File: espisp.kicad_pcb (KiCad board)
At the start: 2 copper layers, 17.1 x 26.7 mm, 20 parts, among them P1 FTDI_BASIC, SW1 SW_PUSH, SW2 SW_PUSH, U1 ESP-12, U2 AMS1117-3.3

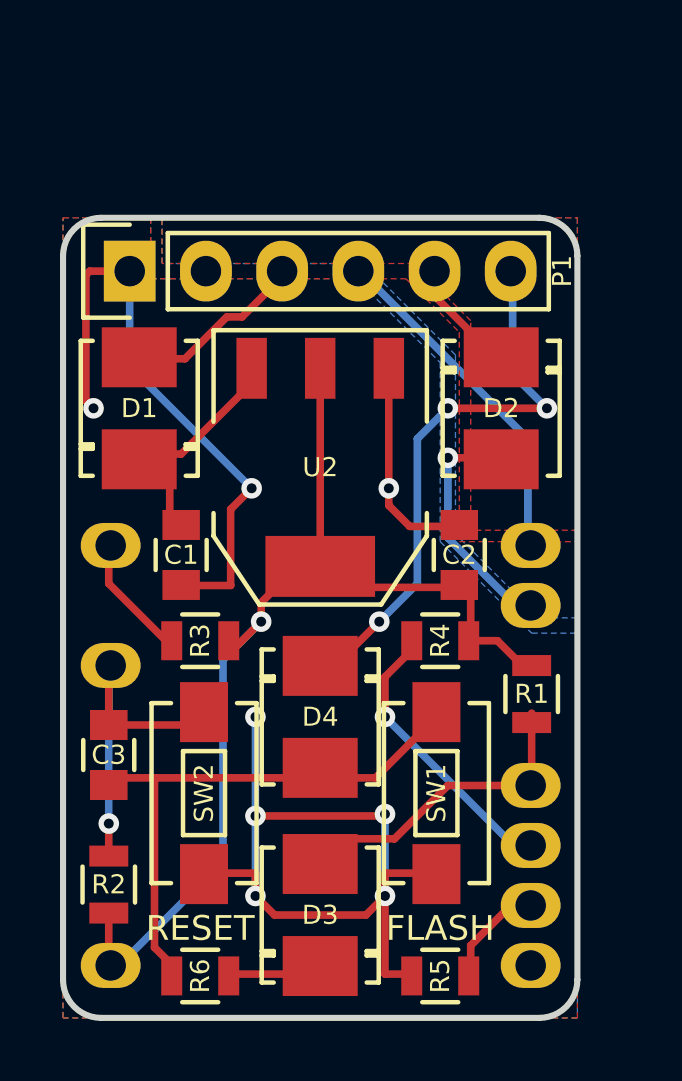
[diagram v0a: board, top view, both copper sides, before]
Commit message: Changed FLASH button to a general GPIO0 button.
First manufacturing.
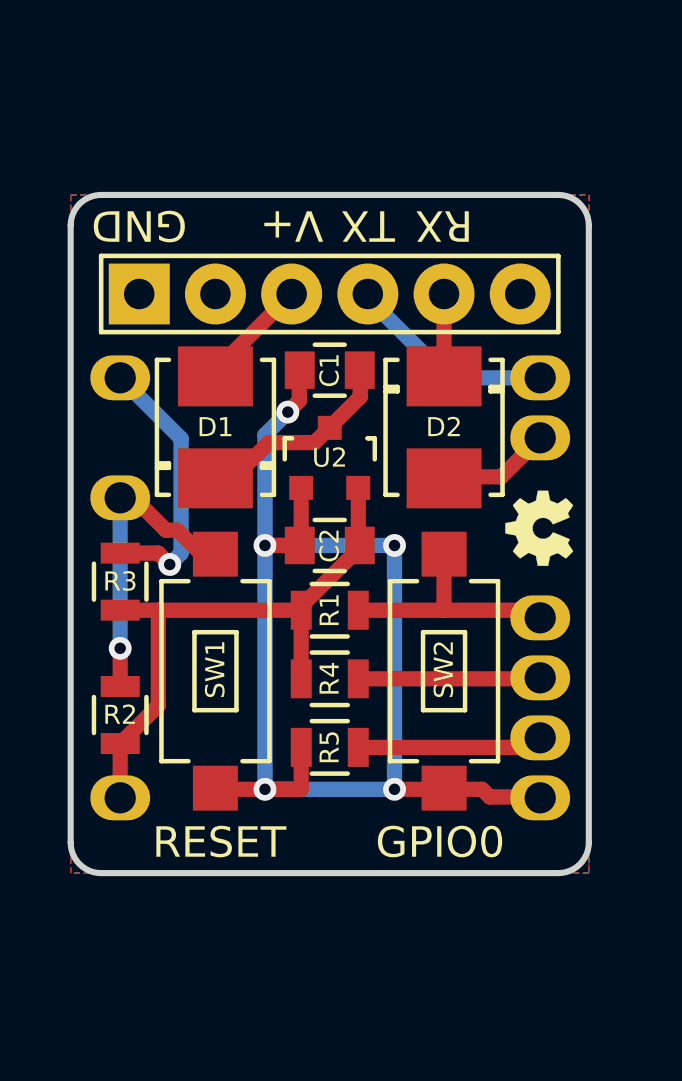
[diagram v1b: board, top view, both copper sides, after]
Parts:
- removed C3: 100nF, Capacitors_SMD:C_0805
- removed D3, D4: 1N4148, Diodes_SMD:DO-214BA
- removed R6: 1K, Resistors_SMD:R_0805
- C1, C2: value CP -> 1uF
- D1, D2: value 1N4148 -> 1N5819
- G***: moved to F.Cu
- P1: footprint Pin_Headers:Pin_Header_Straight_1x06 -> my_footprints:Pin_Header_Simple_1x06
- SW1: value SW_PUSH -> RESET; footprint Buttons_Switches_SMD:SW_SPST_EVQPE1 -> my_footprints:SMD_PUSHBUTTON_3.6x6.0mm
- SW2: value SW_PUSH -> FLASH; footprint Buttons_Switches_SMD:SW_SPST_EVQPE1 -> my_footprints:SMD_PUSHBUTTON_3.6x6.0mm
- U2: value AMS1117-3.3 -> XC6206; footprint TO_SOT_Packages_SMD:SOT-223 -> TO_SOT_Packages_SMD:SOT-23
- moved SW2 8.97 mm to (54.1, 44.3), turned to 0 degrees
- moved R5 8.46 mm to (50.3, 46.9)
- moved SW1 8.41 mm to (46.5, 44.3), turned to 0 degrees
- moved C1 7.90 mm to (50.3, 34.3), turned to 180 degrees
- moved R1 7.29 mm to (50.3, 42.3), turned to 0 degrees
- moved G*** 5.99 mm to (54.5, 39.5), turned to 180 degrees
- moved R2 5.66 mm to (43.3, 45.8)
- moved U1 5.60 mm to (43.3, 34.5)
- moved C2 4.33 mm to (50.3, 40.1), turned to 180 degrees
- moved R4 3.90 mm to (50.3, 44.6), turned to 0 degrees
- moved R3 3.31 mm to (43.3, 41.3), turned to 90 degrees
- moved D1 2.62 mm to (46.5, 36.2)
- moved G*** 2.43 mm to (57.3, 39.6), turned to 90 degrees
- moved D2 2.01 mm to (54.1, 36.2)
- moved P1 0.83 mm to (43.9, 31.8)
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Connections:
- P1 pad 6: /DTR_5V -> (no net)
- SW1 pad 1: Net-(C3-Pad1) -> /CH_PD
- SW2 pad 1: /CH_PD -> /GPIO0
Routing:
- net Net-(C3-Pad1): track 17.0 -> 0.00 mm
- net /DTR_5V: track 16.9 -> 0.00 mm, vias 3 -> 0
- net +3V3: track 33.3 -> 19.8 mm, vias 1 -> 0
- net GND: track 51.1 -> 43.8 mm, vias 8 -> 5
- net /RESET: track 4.14 -> 9.03 mm, vias 0 -> 1
- net /GPIO15: track 2.30 -> 5.97 mm
- net /TXD: track 10.4 -> 7.00 mm
- net /RXD: track 6.30 -> 3.70 mm, vias 1 -> 0
- net /GPIO2: track 8.34 -> 5.97 mm, vias 1 -> 0
- net Net-(D3-Pad1): track 2.03 -> 0.00 mm
- net /VIN_5V: track 4.43 -> 3.05 mm
- net /GPIO0: track 9.25 -> 7.87 mm
- net /CH_PD: track 11.0 -> 10.1 mm
- net Net-(C1-Pad1): track 5.29 -> 5.83 mm
- removed copper zone on B.Cu, net (none)
- removed copper zone on F.Cu, net (none)
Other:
- board size 17.1 x 26.7 mm -> 17.3 x 22.6 mm
- net class Default: clearance 0.2032 -> 0.254; trace_width 0.254 -> 0.508; via_dia 0.6858 -> 0.762; via_drill 0.3302 -> 0.381
- rule trace_clearance: 0.2032 -> 0.254
- board text added: "ESP-ISP"
- board text added: "Rev.4"
- board text added: "V+"
- board text removed: "ESP-12 Antenna"
- board text removed: "ESP-12 ISP"
- board text removed: "FLASH"
- board text removed: "Rv.3"
- board text removed: "VIN"

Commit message: Combine RESET and GPIO0 into one button. (Untested)
Pressing the button should reset the MCU. Pressing and holding the
button for ~5 seconds should make it enter flash mode upon release.

Take a look at /proto/flash.txt to see it in action.
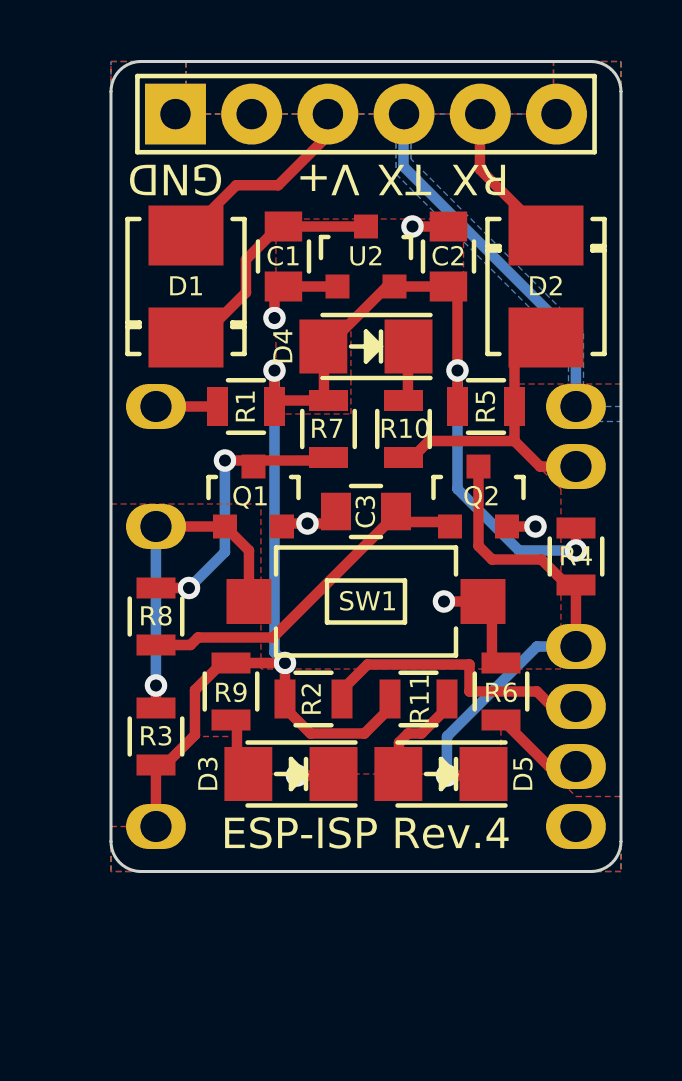
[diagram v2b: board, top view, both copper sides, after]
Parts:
- removed G***: LOGO, my_footprints:Ferret_Logo_0.1in
- removed G***: LOGO, my_footprints:OSHW_Logo_0.1in
- removed SW2: FLASH, my_footprints:SMD_PUSHBUTTON_3.6x6.0mm
- added C3: 2.2uF, Capacitors_SMD:C_0805, F.Cu at (51.5, 39.0)
- added D3: GREEN, LEDs:LED_1206, F.Cu at (49.0, 47.8)
- added D4: GREEN, LEDs:LED_1206, F.Cu at (51.5, 33.5)
- added D5: RED, LEDs:LED_1206, F.Cu at (54.0, 47.8)
- added Q1: 2N7002, TO_SOT_Packages_SMD:SOT-23, F.Cu at (47.8, 38.5)
- added Q2: 2N7002, TO_SOT_Packages_SMD:SOT-23, F.Cu at (55.2, 38.5)
- added R10: 220, Resistors_SMD:R_0805, F.Cu at (52.8, 36.2)
- added R11: 220, Resistors_SMD:R_0805, F.Cu at (53.2, 45.2)
- added R6: 10K, Resistors_SMD:R_0805, F.Cu at (56.0, 45.0)
- added R7: 1M, Resistors_SMD:R_0805, F.Cu at (50.2, 36.2)
- added R8: 1M, Resistors_SMD:R_0805, F.Cu at (44.5, 42.5)
- added R9: 220, Resistors_SMD:R_0805, F.Cu at (47.0, 45.0)
- moved R5 12.5 mm to (55.5, 35.5)
- moved C2 10.4 mm to (54.2, 30.5), turned to 90 degrees
- moved P1 9.65 mm to (51.5, 25.8)
- moved R4 9.16 mm to (58.5, 40.5), turned to 270 degrees
- moved R1 7.34 mm to (47.5, 35.5), turned to 180 degrees
- moved U2 6.82 mm to (51.5, 30.5)
- moved R2 6.47 mm to (49.8, 45.2), turned to 0 degrees
- moved D2 5.80 mm to (57.5, 31.5)
- moved SW1 5.53 mm to (51.5, 42.0), turned to 270 degrees
- moved R3 5.30 mm to (44.5, 46.5), turned to 270 degrees
- moved D1 4.80 mm to (45.5, 31.5)
- moved C1 4.09 mm to (48.8, 30.5), turned to 270 degrees
- moved U1 1.53 mm to (44.5, 35.5)
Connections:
- R1 pad 2: /GPIO0 -> /RESET
- R2 pad 2: /CH_PD -> /GPIO2
- R3 pad 1: +3V3 -> /CH_PD
- R3 pad 2: /RESET -> +3V3
- R4 pad 2: /GPIO2 -> /GPIO0
- R5 pad 1: /GPIO15 -> /RXD
- R5 pad 2: GND -> +3V3
- SW1 pad 1: /CH_PD -> GND
- SW1 pad 2: GND -> /CH_PD
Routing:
- net GND: track 43.8 -> 12.0 mm, vias 5 -> 6
- net +3V3: track 19.8 -> 47.5 mm, vias 0 -> 4
- net Net-(C3-Pad1): track 0.00 -> 11.5 mm
- net Net-(Q1-Pad3): track 0.00 -> 9.25 mm, vias 0 -> 2
- net /GPIO0: track 7.87 -> 16.5 mm, vias 0 -> 1
- net /RESET: track 9.03 -> 2.10 mm, vias 1 -> 0
- net /RXD: track 3.70 -> 9.98 mm
- net /TXD: track 7.00 -> 12.1 mm
- net /GPIO2: track 5.97 -> 9.19 mm
- net Net-(D5-Pad2): track 0.00 -> 3.18 mm
- net /GPIO15: track 5.97 -> 3.09 mm
- net /VIN_5V: track 3.05 -> 5.36 mm
- net /RXD_5V: track 2.29 -> 4.21 mm
- net Net-(C1-Pad1): track 5.83 -> 7.68 mm
- net Net-(D4-Pad1): track 0.00 -> 1.80 mm
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- added copper zone on B.Cu, net (none)
- added copper zone on F.Cu, net (none)
- removed copper zone on F.Cu, net GND
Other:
- board size 17.3 x 22.6 mm -> 17 x 27 mm
- net class Default: clearance 0.254 -> 0.175; trace_width 0.508 -> 0.35; via_dia 0.762 -> 0.75; via_drill 0.381 -> 0.4
- rule trace_clearance: 0.254 -> 0.175
- rule trace_min: 0.1524 -> 0.175
- rule via_min_drill: 0.3302 -> 0.4
- rule via_min_size: 0.6858 -> 0.75
- board text added: "ESP-ISP Rev.4"
- board text removed: "ESP-ISP"
- board text removed: "Rev.4"
